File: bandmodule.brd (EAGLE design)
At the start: 35.5 x 41.3 mm, 16 parts

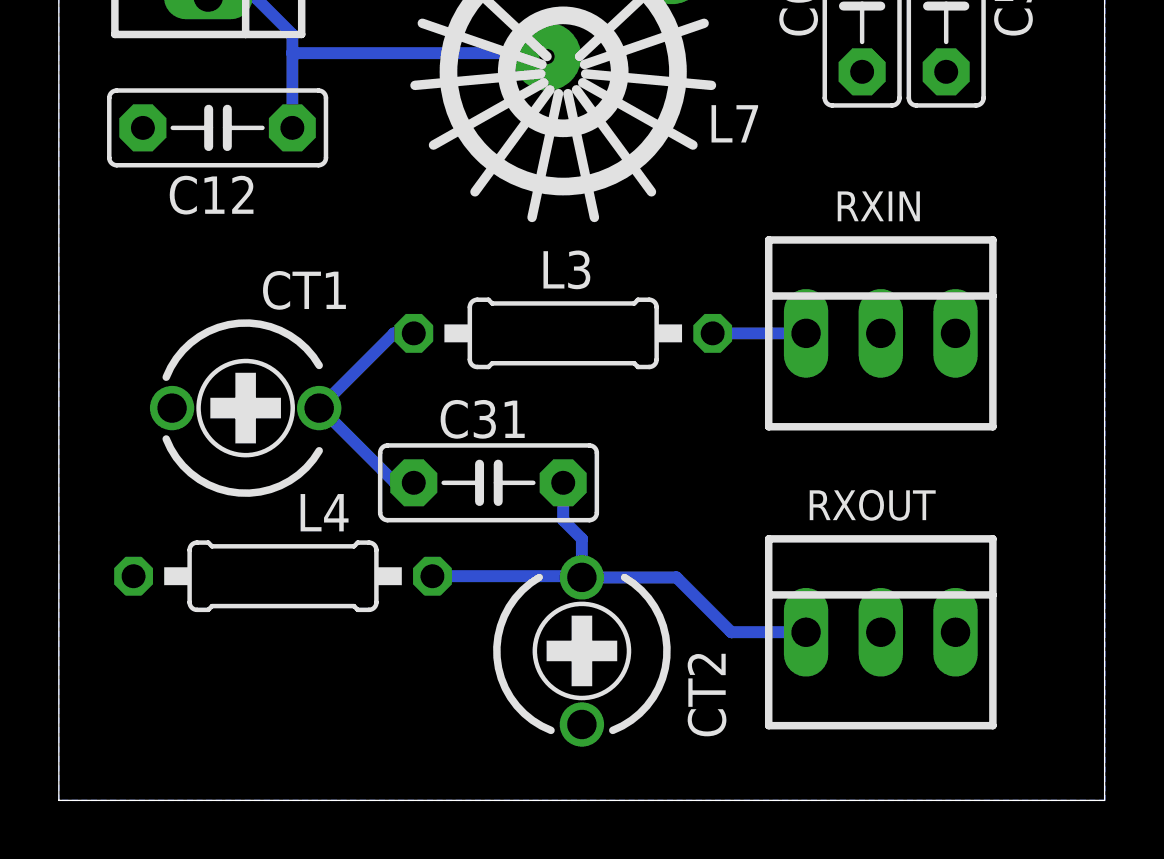
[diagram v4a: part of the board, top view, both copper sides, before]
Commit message: Move RX around for larger board note rectangle
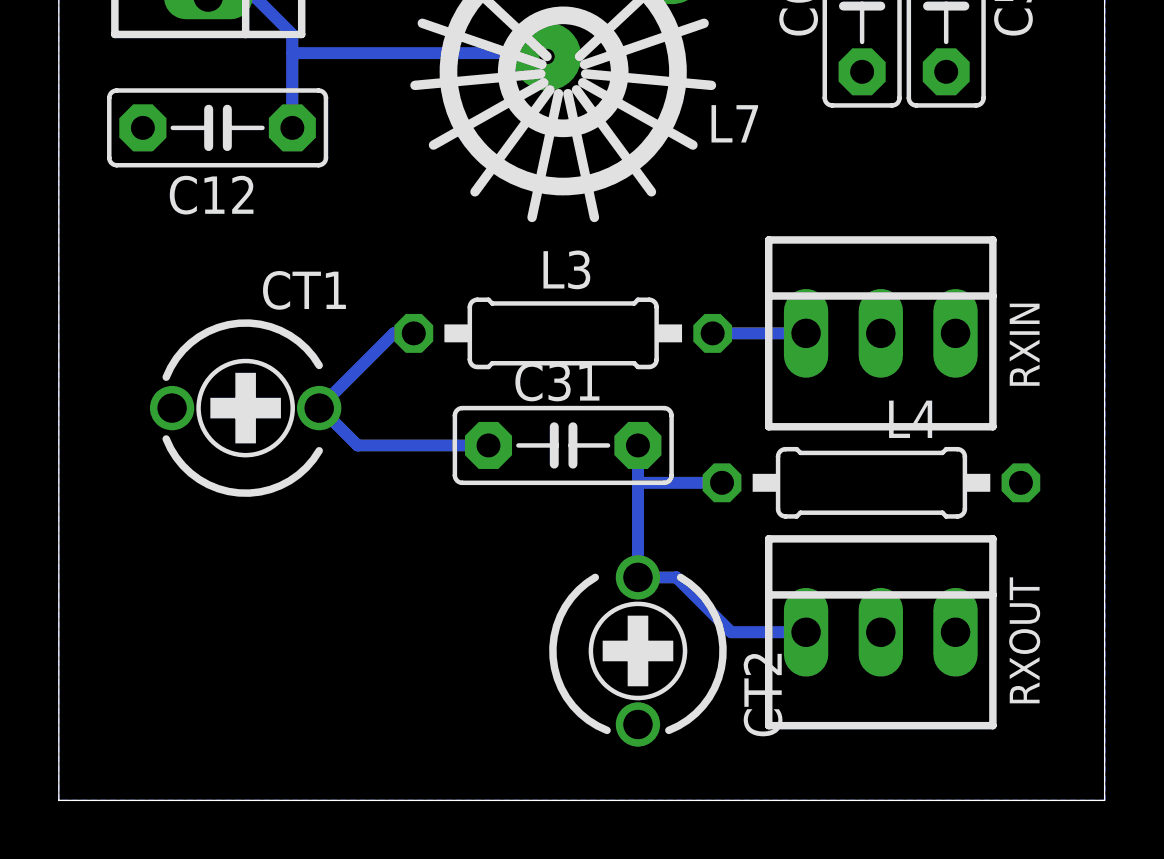
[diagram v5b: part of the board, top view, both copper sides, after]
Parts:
- moved L4 20.3 mm to (27.6, 10.8)
- moved C31 2.84 mm to (17.1, 12.1)
- moved CT2 1.90 mm to (19.7, 5.08)
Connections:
- net GND: now also L4.2; no longer L4.1
- net N$4: now also L4.1; no longer L4.2
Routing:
- net N$4: track 17.0 -> 13.8 mm
- net N$2: track 8.53 -> 10.6 mm
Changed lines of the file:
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@@
 <wire x1="35.5475" y1="41.265" x2="0" y2="41.265" width="0" layer="20"/>
 <wire x1="0" y1="41.265" x2="0" y2="0" width="0" layer="20"/>
-<rectangle x1="1.5875" y1="1.5875" x2="13.97" y2="6.0325" layer="51"/>
+<rectangle x1="1.5875" y1="1.5875" x2="15.875" y2="9.525" layer="51"/>
 </plain>
 <attributes>
@@
 <attribute name="NAME" x="29.1465" y="37.2745" size="1.27" layer="25" ratio="10" rot="R270"/>
 </element>
-<element name="C31" library="capacitor-wima" package="C5B2.5" value="5p" x="14.605" y="10.795" smashed="yes">
-<attribute name="NAME" x="12.8905" y="12.319" size="1.27" layer="25" ratio="10"/>
+<element name="C31" library="capacitor-wima" package="C5B2.5" value="5p" x="17.145" y="12.065" smashed="yes">
+<attribute name="NAME" x="15.4305" y="13.589" size="1.27" layer="25" ratio="10"/>
 </element>
 <element name="C5" library="capacitor-wima" package="C5B2.5" value="330p" x="30.1625" y="27.305" smashed="yes" rot="R90">
@@
 <attribute name="NAME" x="9.9025" y="17.9725" size="1.27" layer="25" rot="R180"/>
 </element>
-<element name="CT2" library="rcl" package="CTRIMTZ03" value="60p" x="17.78" y="5.08" smashed="yes" rot="R180">
-<attribute name="NAME" x="21.3975" y="5.14" size="1.27" layer="25" rot="R270"/>
+<element name="CT2" library="rcl" package="CTRIMTZ03" value="60p" x="19.685" y="5.08" smashed="yes" rot="R180">
+<attribute name="NAME" x="23.3025" y="5.14" size="1.27" layer="25" rot="R270"/>
 </element>
 <element name="L7" library="toroids" package="T30-2-28AWG-12T" value="T30-2 / 12T" x="17.145" y="24.765" smashed="yes" rot="R180">
@@
 <attribute name="MF" value="MOLEX" x="27.94" y="15.875" size="1.778" layer="27" display="off"/>
 <attribute name="MPN" value="22-23-2031" x="27.94" y="15.875" size="1.778" layer="27" display="off"/>
-<attribute name="NAME" x="26.3525" y="19.685" size="1.016" layer="25" ratio="10"/>
+<attribute name="NAME" x="33.3375" y="13.97" size="1.016" layer="25" ratio="10" rot="R90"/>
 <attribute name="OC_FARNELL" value="1462950" x="27.94" y="15.875" size="1.778" layer="27" display="off"/>
 <attribute name="OC_NEWARK" value="30C0862" x="27.94" y="15.875" size="1.778" layer="27" display="off"/>
@@
 <attribute name="MF" value="MOLEX" x="27.94" y="5.715" size="1.778" layer="27" display="off"/>
 <attribute name="MPN" value="22-23-2031" x="27.94" y="5.715" size="1.778" layer="27" display="off"/>
-<attribute name="NAME" x="25.4" y="9.525" size="1.016" layer="25" ratio="10"/>
+<attribute name="NAME" x="33.3375" y="3.175" size="1.016" layer="25" ratio="10" rot="R90"/>
 <attribute name="OC_FARNELL" value="1462950" x="27.94" y="5.715" size="1.778" layer="27" display="off"/>
 <attribute name="OC_NEWARK" value="30C0862" x="27.94" y="5.715" size="1.778" layer="27" display="off"/>
@@
 <attribute name="OC_NEWARK" value="25C3832" x="5.08" y="28.575" size="1.778" layer="27" rot="R270" display="off"/>
 </element>
-<element name="L4" library="eagle-ltspice" package="0207/10" value="5.6uH" x="7.62" y="7.62" smashed="yes">
-<attribute name="NAME" x="8.0645" y="9.144" size="1.27" layer="25" ratio="10"/>
-<attribute name="SPICEMODEL" value="NONE" x="7.62" y="7.62" size="1.778" layer="27" display="off"/>
-<attribute name="SPICEPREFIX" value="L" x="7.62" y="7.62" size="1.778" layer="27" display="off"/>
+<element name="L4" library="eagle-ltspice" package="0207/10" value="5.6uH" x="27.6225" y="10.795" smashed="yes">
+<attribute name="NAME" x="28.067" y="12.319" size="1.27" layer="25" ratio="10"/>
+<attribute name="SPICEMODEL" value="NONE" x="27.6225" y="10.795" size="1.778" layer="27" display="off"/>
+<attribute name="SPICEPREFIX" value="L" x="27.6225" y="10.795" size="1.778" layer="27" display="off"/>
 </element>
 <element name="L3" library="eagle-ltspice" package="0207/10" value="5.6uH" x="17.145" y="15.875" smashed="yes">
@@
 <contactref element="C31" pad="2"/>
 <contactref element="CT2" pad="2"/>
-<contactref element="L4" pad="2"/>
-<wire x1="17.145" y1="10.795" x2="17.145" y2="9.525" width="0.4064" layer="16"/>
-<wire x1="17.145" y1="9.525" x2="17.78" y2="8.89" width="0.4064" layer="16"/>
-<wire x1="17.78" y1="8.89" x2="17.78" y2="7.58" width="0.4064" layer="16"/>
-<wire x1="12.7" y1="7.62" x2="17.74" y2="7.62" width="0.4064" layer="16"/>
-<wire x1="17.74" y1="7.62" x2="17.78" y2="7.58" width="0.4064" layer="16"/>
-<wire x1="17.78" y1="7.58" x2="20.995" y2="7.58" width="0.4064" layer="16"/>
+<contactref element="L4" pad="1"/>
+<wire x1="19.685" y1="7.58" x2="20.995" y2="7.58" width="0.4064" layer="16"/>
 <wire x1="20.995" y1="7.58" x2="22.86" y2="5.715" width="0.4064" layer="16"/>
 <wire x1="22.86" y1="5.715" x2="25.4" y2="5.715" width="0.4064" layer="16"/>
+<wire x1="19.685" y1="10.795" x2="19.685" y2="12.065" width="0.4064" layer="16"/>
+<wire x1="19.685" y1="10.795" x2="19.685" y2="7.58" width="0.4064" layer="16"/>
+<wire x1="22.5425" y1="10.795" x2="19.685" y2="10.795" width="0.4064" layer="16"/>
 </signal>
 <signal name="GND">
@@
 <contactref element="C5" pad="1"/>
 <contactref element="C12" pad="1"/>
-<contactref element="L4" pad="1"/>
+<contactref element="L4" pad="2"/>
 <polygon width="0.4064" layer="16">
 <vertex x="0" y="40.64"/>
@@
 <wire x1="11.39" y1="15.875" x2="8.85" y2="13.335" width="0.4064" layer="16"/>
 <wire x1="8.85" y1="13.335" x2="8.89" y2="13.335" width="0.4064" layer="16"/>
-<wire x1="8.89" y1="13.335" x2="11.43" y2="10.795" width="0.4064" layer="16"/>
-<wire x1="11.43" y1="10.795" x2="12.065" y2="10.795" width="0.4064" layer="16"/>
+<wire x1="8.85" y1="13.335" x2="8.89" y2="13.335" width="0.4064" layer="16"/>
+<wire x1="8.89" y1="13.335" x2="10.16" y2="12.065" width="0.4064" layer="16"/>
+<wire x1="10.16" y1="12.065" x2="14.605" y2="12.065" width="0.4064" layer="16"/>
 </signal>
 <signal name="N$5">
